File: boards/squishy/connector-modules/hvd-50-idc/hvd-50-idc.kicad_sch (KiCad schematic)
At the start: 14 parts, among them J1 SCSI PHY Mezz, J2 Conn_02x25_Odd_Even, J3 Conn_01x04, J4 Conn_02x34_Clockwise_Shield, J5 Conn_02x24_Clockwise_Shield, U1 M24C02-RMC

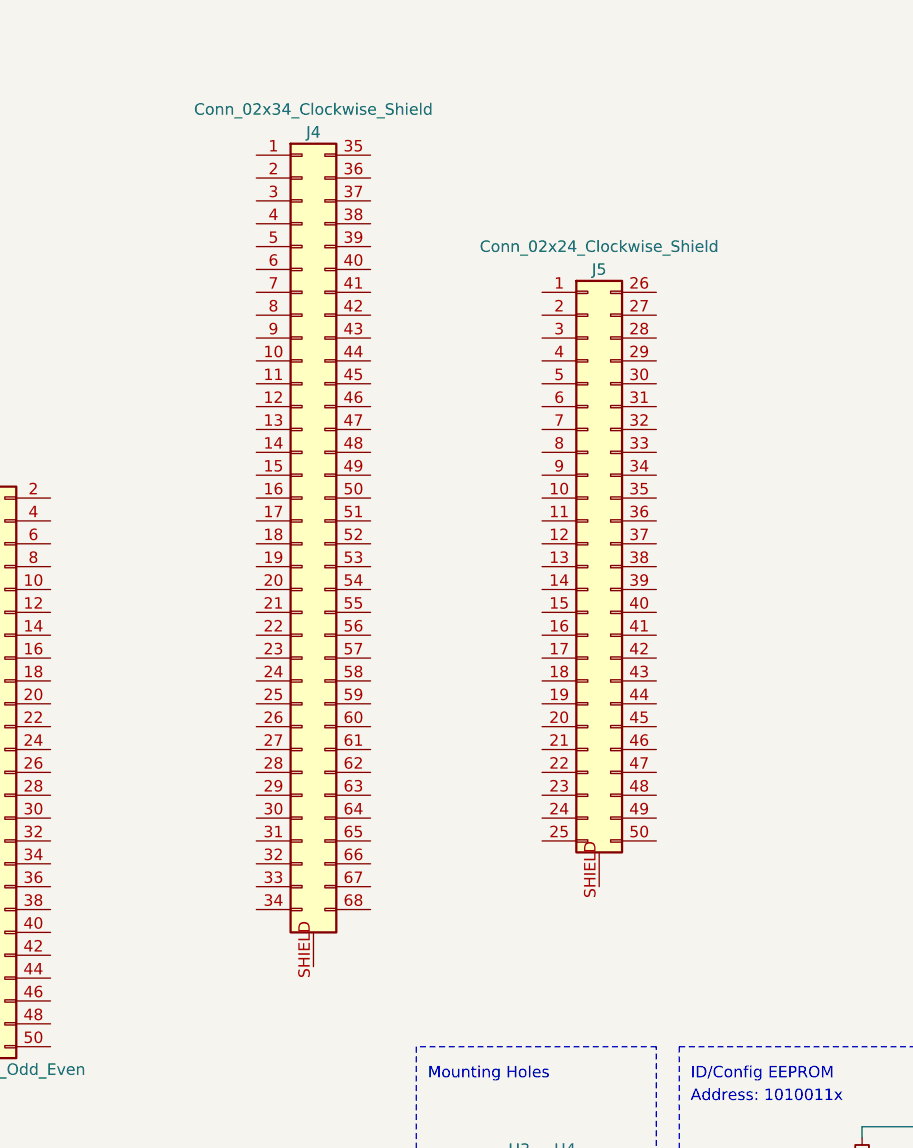
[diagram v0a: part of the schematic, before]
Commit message: squishy: connectors: Removed unneeded connector symbols in the given kicad schematics
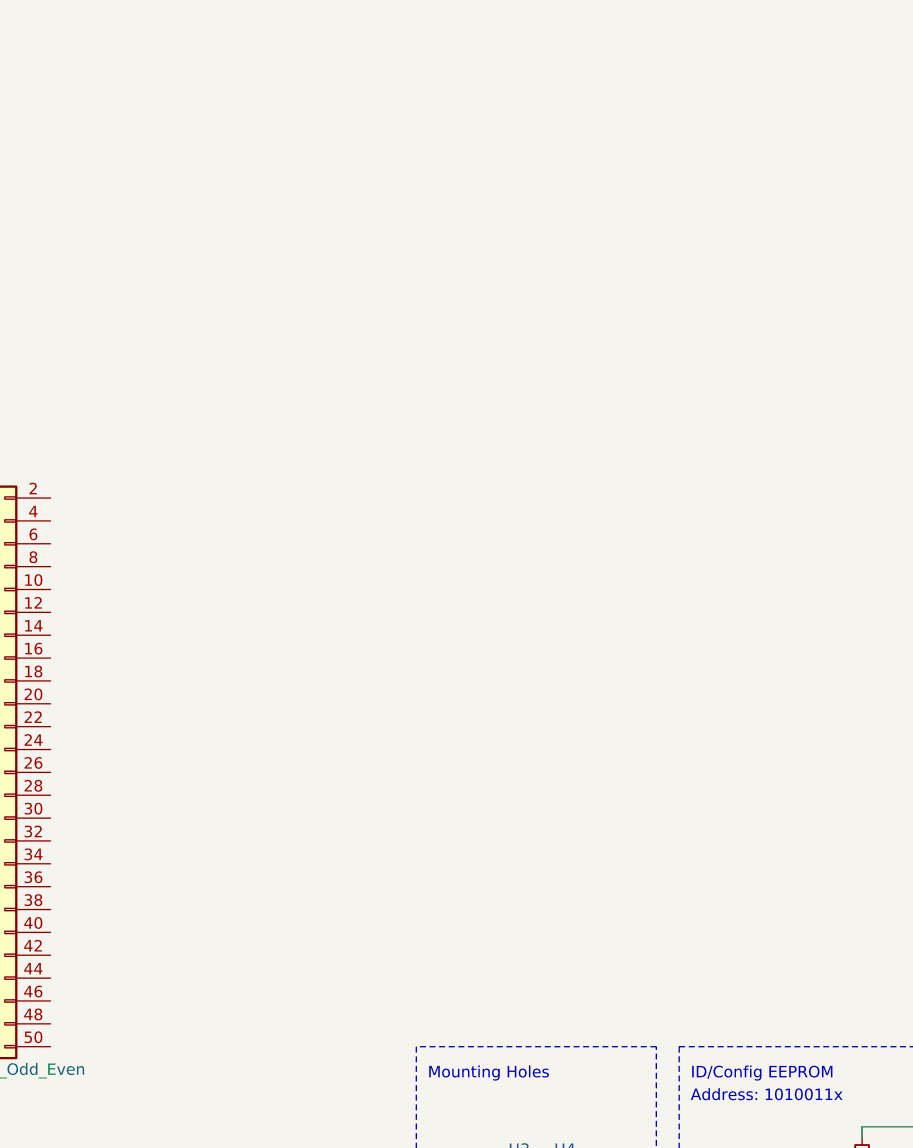
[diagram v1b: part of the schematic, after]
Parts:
- removed J4: Conn_02x34_Clockwise_Shield, symbol lethalbit-connectors:Conn_02x34_Counter_Clockwise
- removed J5: Conn_02x24_Clockwise_Shield, symbol lethalbit-connectors:Conn_02x25_Counter_Clockwise

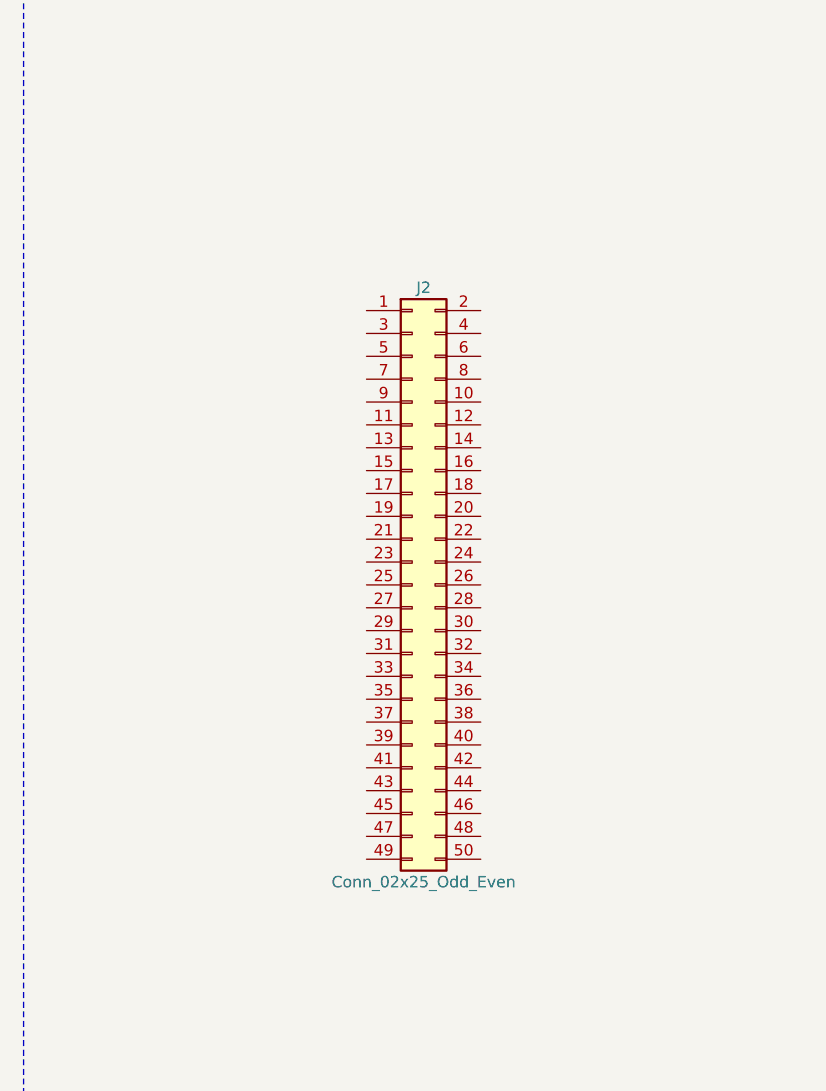
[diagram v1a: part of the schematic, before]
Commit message: squishy: connectors: hooked up hd-50-idc connector
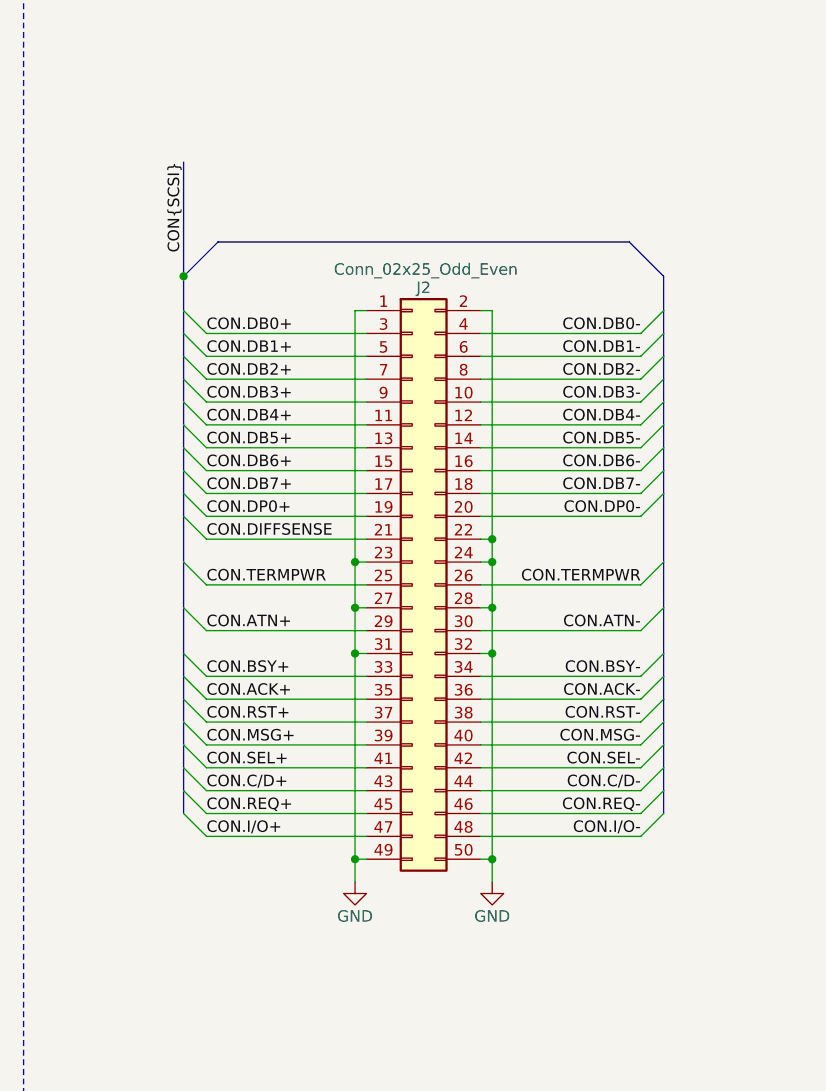
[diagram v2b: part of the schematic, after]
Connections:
- net CON.ACK+: now also J2.35 (Pin_35)
- net CON.ACK-: now also J2.36 (Pin_36)
- net CON.ATN+: now also J2.29 (Pin_29)
- net CON.ATN-: now also J2.30 (Pin_30)
- net CON.BSY+: now also J2.33 (Pin_33)
- net CON.BSY-: now also J2.34 (Pin_34)
- net CON.C/D+: now also J2.43 (Pin_43)
- net CON.C/D-: now also J2.44 (Pin_44)
- net CON.DB0+: now also J2.3 (Pin_3)
- net CON.DB0-: now also J2.4 (Pin_4)
- net CON.DB1+: now also J2.5 (Pin_5)
- net CON.DB1-: now also J2.6 (Pin_6)
- net CON.DB2+: now also J2.7 (Pin_7)
- net CON.DB2-: now also J2.8 (Pin_8)
- net CON.DB3+: now also J2.9 (Pin_9)
- net CON.DB3-: now also J2.10 (Pin_10)
- net CON.DB4+: now also J2.11 (Pin_11)
- net CON.DB4-: now also J2.12 (Pin_12)
- net CON.DB5+: now also J2.13 (Pin_13)
- net CON.DB5-: now also J2.14 (Pin_14)
- net CON.DB6+: now also J2.15 (Pin_15)
- net CON.DB6-: now also J2.16 (Pin_16)
- net CON.DB7+: now also J2.17 (Pin_17)
- net CON.DB7-: now also J2.18 (Pin_18)
- net CON.DIFFSENSE: now also J2.21 (Pin_21)
- net CON.DP0+: now also J2.19 (Pin_19)
- net CON.DP0-: now also J2.20 (Pin_20)
- net CON.I/O+: now also J2.47 (Pin_47)
- net CON.I/O-: now also J2.48 (Pin_48)
- net CON.MSG+: now also J2.39 (Pin_39)
- net CON.MSG-: now also J2.40 (Pin_40)
- net CON.REQ+: now also J2.45 (Pin_45)
- net CON.REQ-: now also J2.46 (Pin_46)
- net CON.RST+: now also J2.37 (Pin_37)
- net CON.RST-: now also J2.38 (Pin_38)
- net CON.SEL+: now also J2.41 (Pin_41)
- net CON.SEL-: now also J2.42 (Pin_42)
- net CON.TERMPWR: now also J2.25 (Pin_25), J2.26 (Pin_26)
- net GND: now also J2.1 (Pin_1), J2.2 (Pin_2), J2.22 (Pin_22), J2.23 (Pin_23), J2.24 (Pin_24), J2.27 (Pin_27), J2.28 (Pin_28), J2.31 (Pin_31), J2.32 (Pin_32), J2.49 (Pin_49), J2.50 (Pin_50)

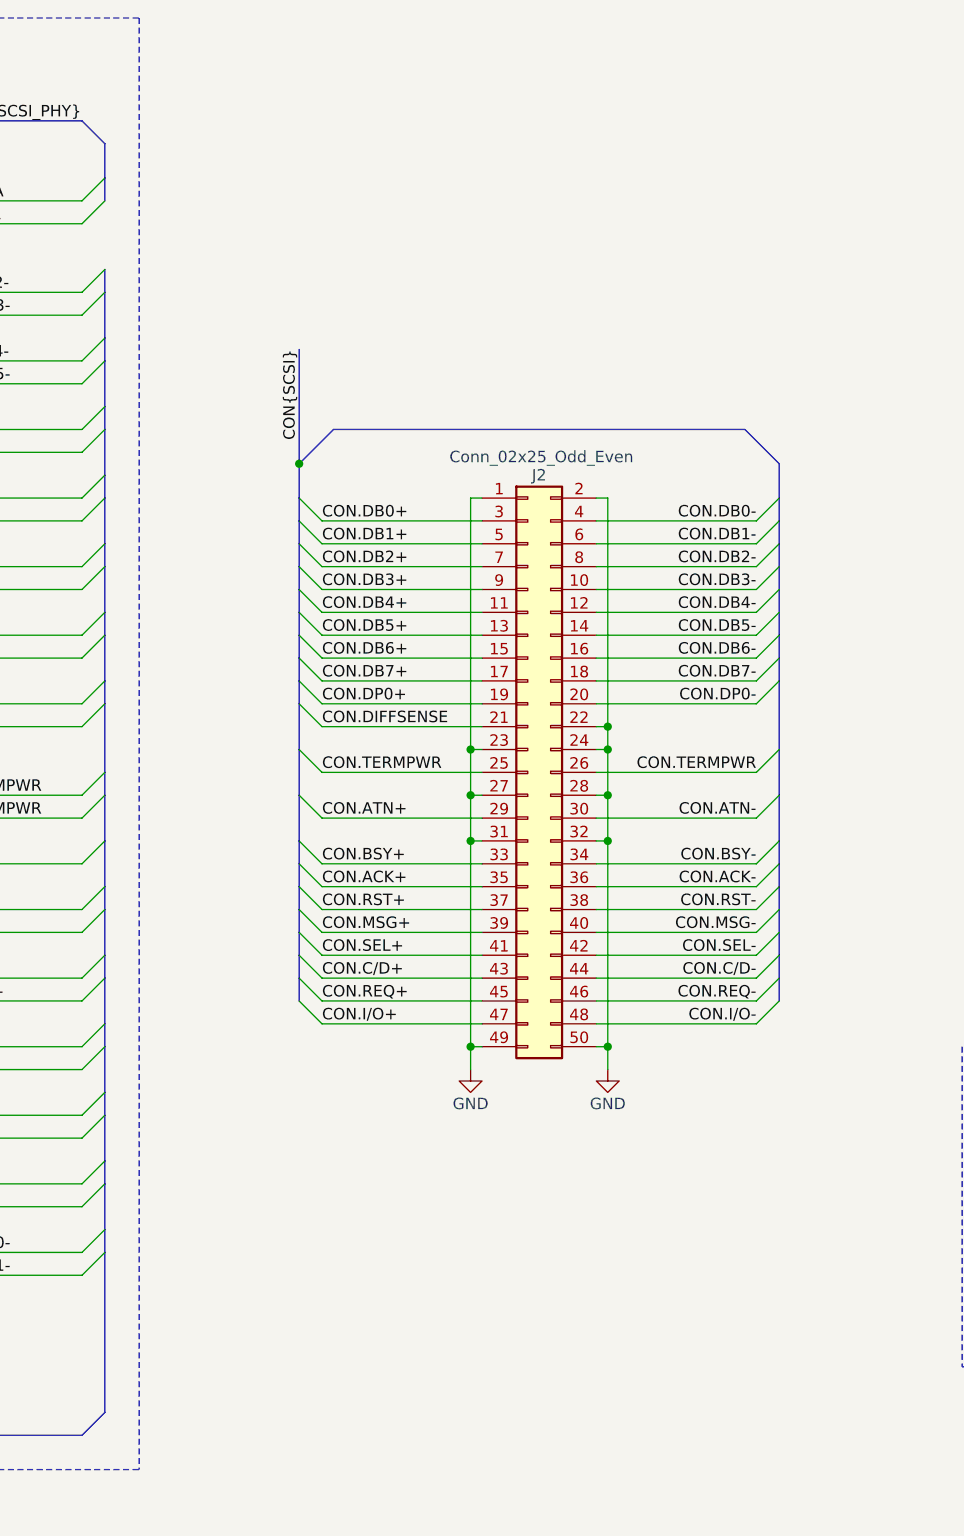
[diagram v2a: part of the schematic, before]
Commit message: squishy: connectors: Cleaned up and unified look/feel of connector schematics
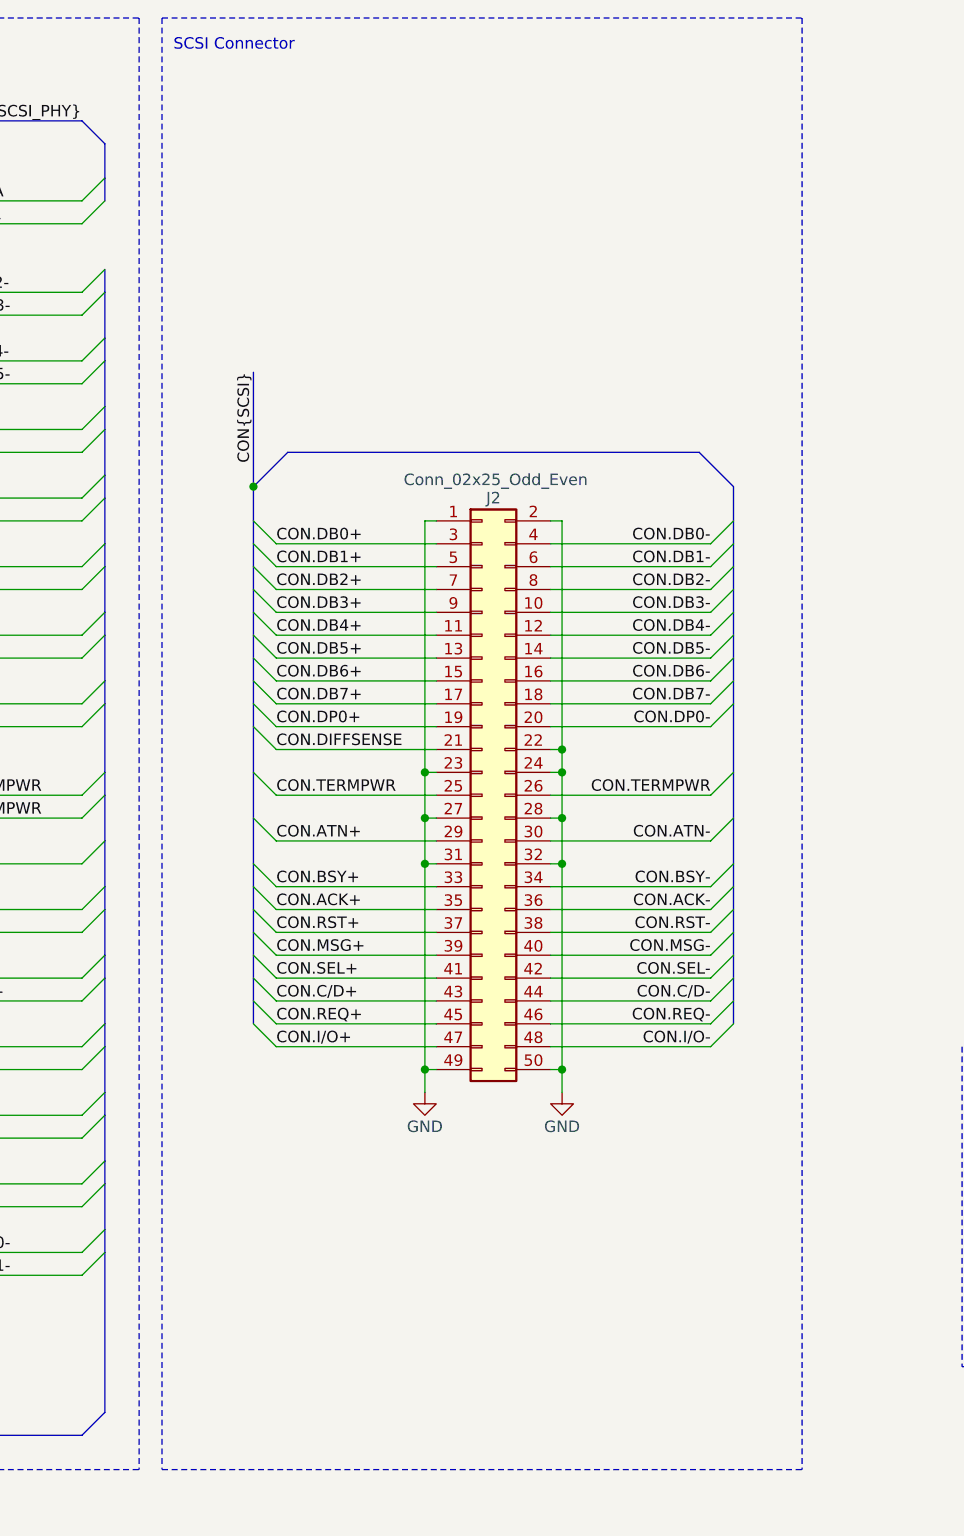
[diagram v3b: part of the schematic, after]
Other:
- note added: "SCSI Connector"
- moved on the sheet: J2

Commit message: squishy: connectors: updated schematic title blocks for connectors as appropriate
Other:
- title: Squishy -  ICD 50 -> Squishy -  SCSI HVD IDC 50 Connector Module
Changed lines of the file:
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@@
 	(paper "A4")
 	(title_block
-		(title "Squishy -  ICD 50")
-		(date "2024-08-22")
+		(title "Squishy -  SCSI HVD IDC 50 Connector Module")
+		(date "2024-09-17")
 		(rev "1")
 		(company "Shrine Maiden Heavy Industries")

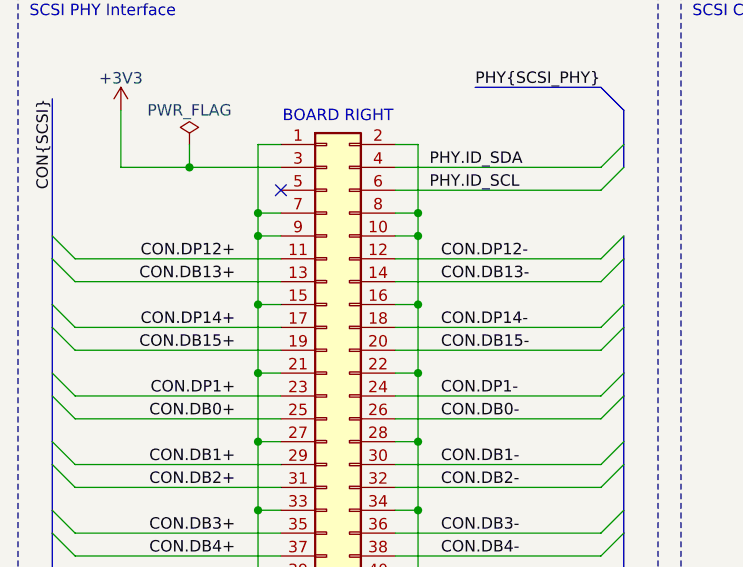
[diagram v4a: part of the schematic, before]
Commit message: squishy: connectors: s/DP12/DB12/g s/DP14/DB14/g
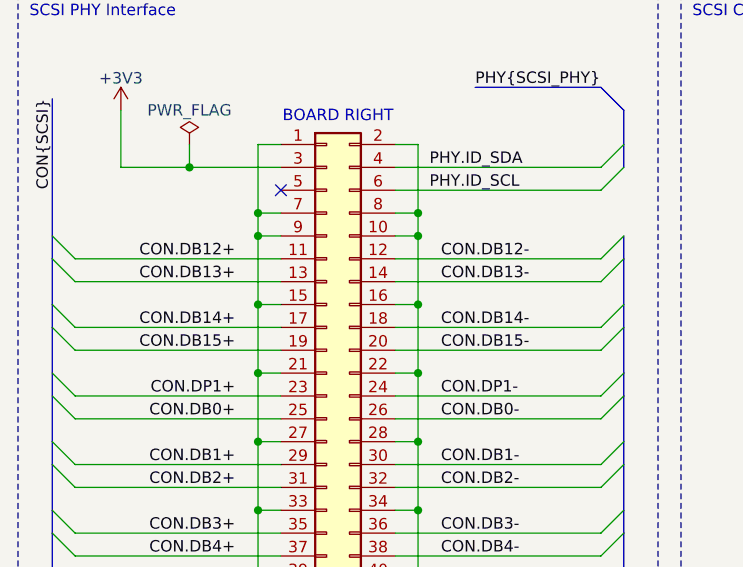
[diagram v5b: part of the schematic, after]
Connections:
- net CON.DP12+ renamed CON.DB12+
- net CON.DP12- renamed CON.DB12-
- net CON.DP14+ renamed CON.DB14+
- net CON.DP14- renamed CON.DB14-
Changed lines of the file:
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@@
 		)
 	)
-	(label "CON.DP14-"
+	(label "CON.DB14-"
 		(at 60.96 52.07 0)
 		(fields_autoplaced yes)
@@
 		)
 	)
-	(label "CON.DP12+"
+	(label "CON.DB12+"
 		(at 38.1 44.45 180)
 		(fields_autoplaced yes)
@@
 		)
 	)
-	(label "CON.DP12-"
+	(label "CON.DB12-"
 		(at 60.96 44.45 0)
 		(fields_autoplaced yes)
@@
 		)
 	)
-	(label "CON.DP14+"
+	(label "CON.DB14+"
 		(at 38.1 52.07 180)
 		(fields_autoplaced yes)
